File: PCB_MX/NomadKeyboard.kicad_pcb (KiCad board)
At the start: 2 copper layers, 159.9 x 129.6 mm, 97 parts, among them J1 4PIN, J2 OLED, SW1 SW_PUSH_LED, SW10 SW_PUSH_LED, SW11 SW_PUSH_LED, SW12 SW_PUSH_LED, SW13 SW_PUSH_LED, SW14 SW_PUSH_LED, SW15 SW_PUSH_LED, SW16 SW_PUSH_LED, SW17 SW_PUSH_LED, SW18 SW_PUSH_LED, SW19 SW_PUSH_LED, SW2 SW_PUSH_LED, SW20 SW_PUSH_LED, SW21 SW_PUSH_LED, SW22 SW_PUSH_LED, SW23 SW_PUSH_LED, SW24 SW_PUSH_LED, SW25 SW_PUSH_LED, SW26 SW_PUSH_LED, SW27 SW_PUSH_LED, SW28 SW_PUSH_LED, SW29 SW_PUSH_LED, SW3 SW_PUSH_LED, SW30 SW_PUSH_LED, SW31 SW_PUSH_LED, SW32 SW_PUSH_LED, SW33 SW_PUSH_LED, SW34 SW_PUSH_LED, SW4 SW_PUSH_LED, SW5 SW_PUSH_LED, SW6 SW_PUSH_LED, SW7 SW_PUSH_LED, SW8 SW_PUSH_LED, SW9 SW_PUSH_LED, U1 ProMicro

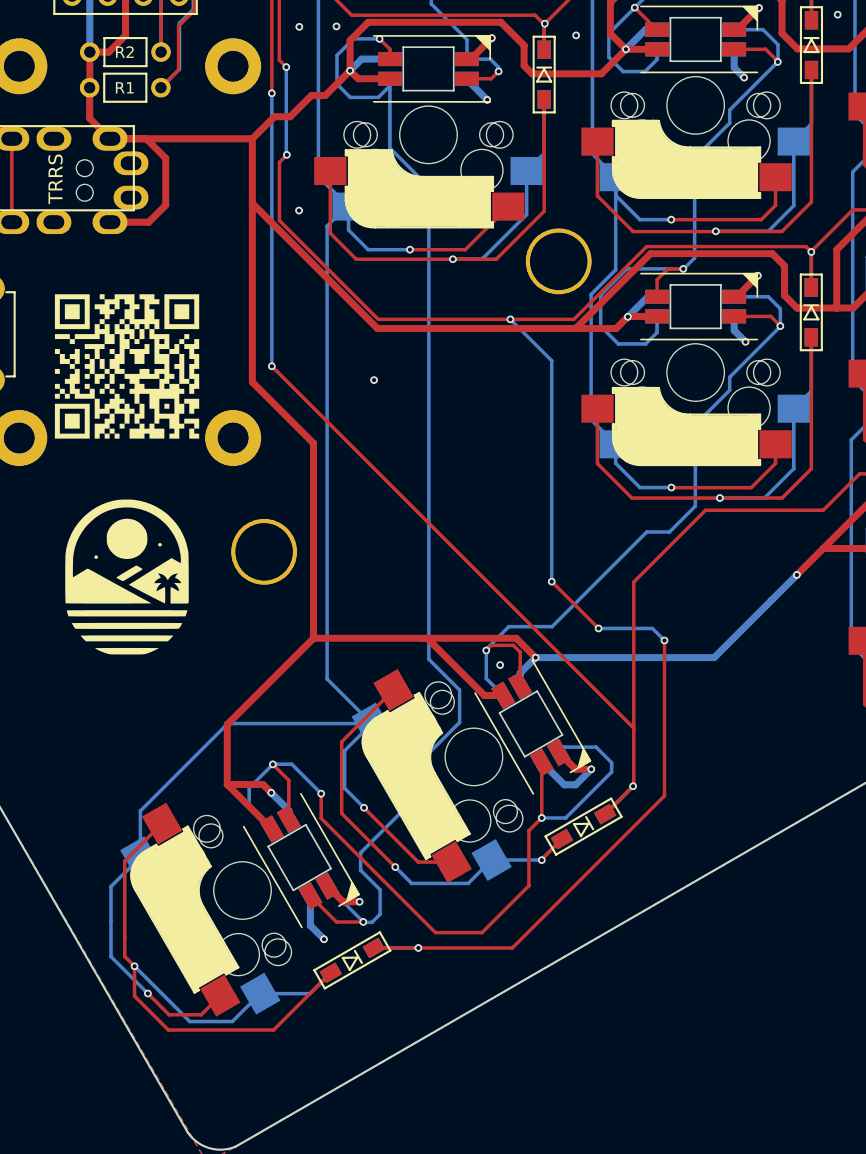
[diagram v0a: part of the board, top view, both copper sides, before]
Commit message: Rotated thumb cluster keys on the MX version for 1.5U shine-through blank key caps
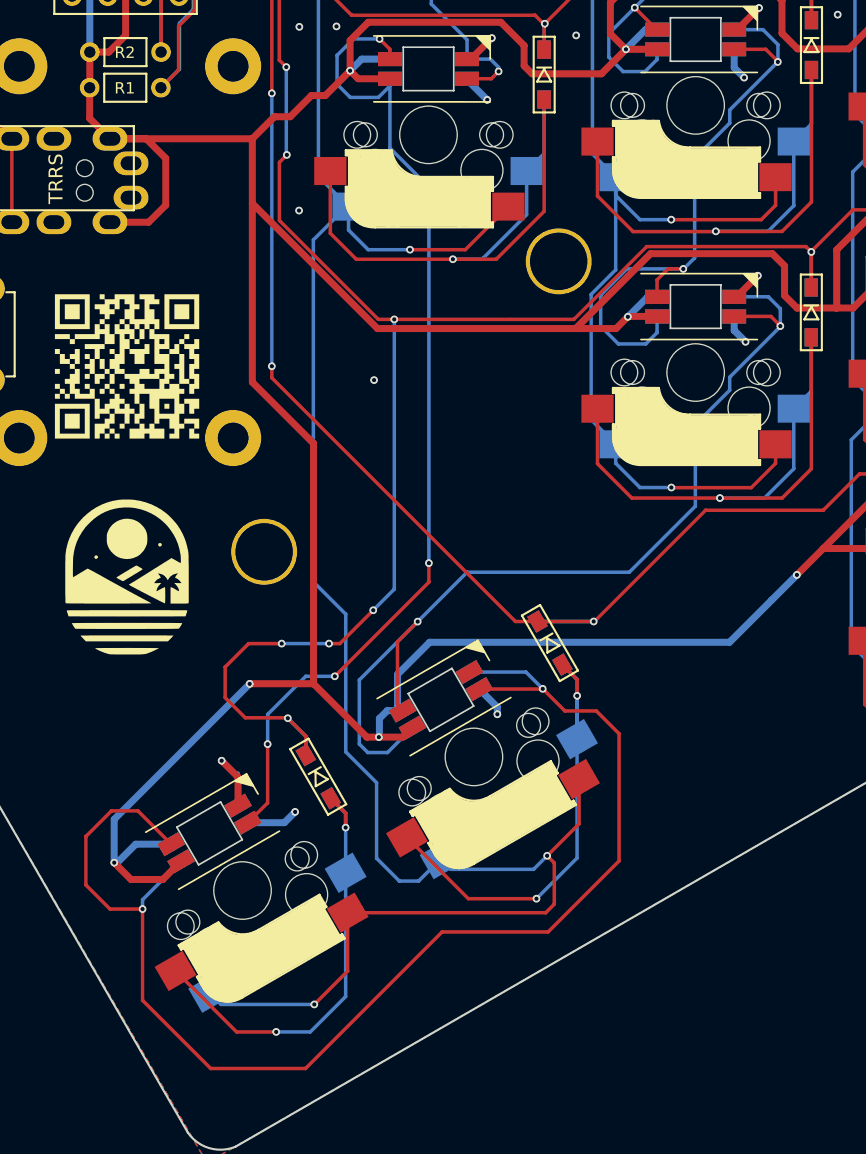
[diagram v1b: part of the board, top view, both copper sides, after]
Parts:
- moved D22 13.3 mm to (93.6, 136.0), turned to -60 degrees
- moved D29 13.3 mm to (110.1, 126.4), turned to -60 degrees
- turned SW22 to -150 degrees
- turned SW29 to -150 degrees
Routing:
- net Net-(SW22B-DOUT): track 56.5 -> 95.3 mm, vias 3 -> 2
- net ROW3: track 284.9 -> 262.9 mm
- net ROW4: track 247.1 -> 229.4 mm
- net Net-(SW23B-DIN): track 51.9 -> 69.3 mm
- net Net-(D22-A): track 47.4 -> 32.1 mm, vias 1 -> 2
- net Net-(SW15B-DOUT): track 86.6 -> 74.9 mm, vias 2 -> 4
- net VCC: track 1349.3 -> 1360.3 mm, vias 49 -> 50
- net COL6: track 206.3 -> 215.8 mm
- net Net-(D29-A): track 31.5 -> 38.2 mm
- net GND: track 180.0 -> 176.0 mm, vias 125 -> 124

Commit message: Update Gerber files for MX version
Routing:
- net Net-(SW15B-DOUT): track 74.9 -> 77.9 mm
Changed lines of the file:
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@@
+	)
+	(segment
+		(start 87.91027 135.71149)
+		(end 87.96027 135.71149)
+		(width 0.25)
+		(layer "B.Cu")
+		(net 63)
 	)
 	(segment
@@
 		(width 0.25)
 		(layer "B.Cu")
+		(net 63)
+	)
+	(segment
+		(start 87.96027 135.71149)
+		(end 90.01912 133.65264)
+		(width 0.25)
+		(layer "B.Cu")

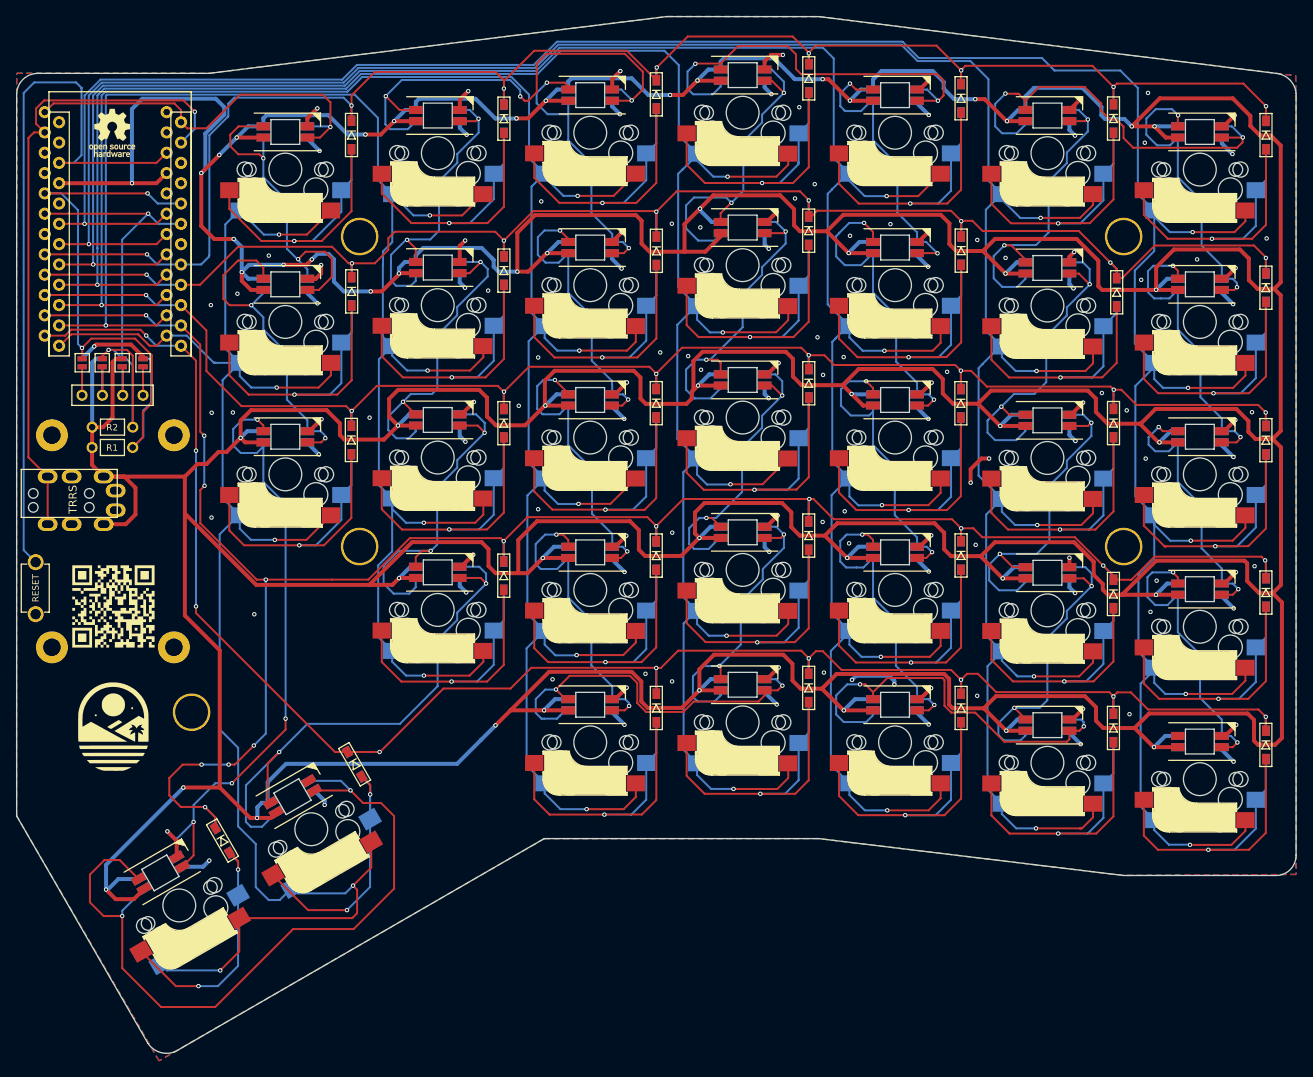
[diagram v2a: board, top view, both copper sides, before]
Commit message: Nomad Rev 2
* Exclusively supports RP2040 CE microcontrollers
* Only one set of headers for hte RP2040 with solder jumpers to select
  the half
* EC12 low-profile rotary encoder support
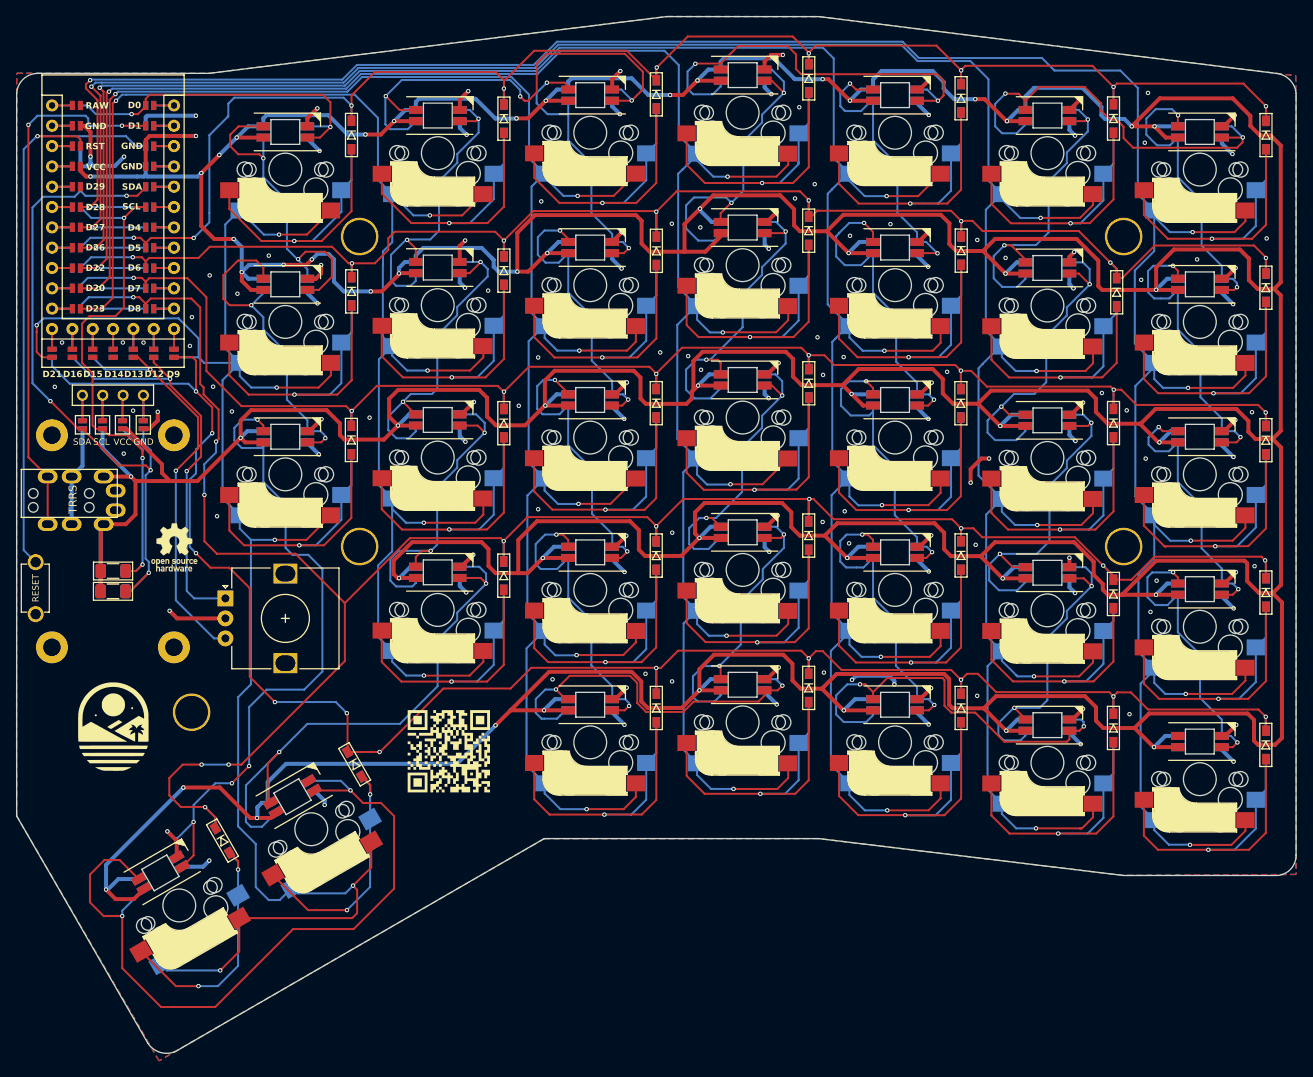
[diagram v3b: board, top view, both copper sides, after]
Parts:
- removed U1: ProMicro, SofleChoc:ProMicro
- added RE1: RotaryEncoder, Rotary_Encoder:RotaryEncoder_Alps_EC12E_Vertical_H20mm, F.Cu at (94.0, 105.7)
- added RP2040_CE1: ~, Nomad:RP2040_CE, F.Cu at (80.0, 57.8)
- R1, R2: footprint SofleChoc:RESISTOR_mini -> Nomad:R_1206_3216Metric_Pad1.30x1.75mm_HandSolder
- moved OH2 52.4 mm to (87.6, 99.3)
- moved OH1 52.4 mm to (87.6, 99.3)
- moved QR2 45.7 mm to (121.9, 124.8)
- moved QR1 45.7 mm to (121.9, 124.8)
- moved R1 18.0 mm to (79.9, 104.8)
- moved R2 18.0 mm to (80.0, 102.3)
- moved JP1 7.76 mm to (83.7, 84.0), turned to -90 degrees
- moved JP2 7.76 mm to (81.1, 84.0), turned to -90 degrees
- moved JP3 7.76 mm to (78.6, 84.0), turned to -90 degrees
- moved JP4 7.76 mm to (76.1, 84.0), turned to -90 degrees
- moved JP5 7.75 mm to (83.7, 84.0), turned to -90 degrees
- moved JP6 7.75 mm to (81.1, 84.0), turned to -90 degrees
- moved JP7 7.75 mm to (78.6, 84.0), turned to -90 degrees
- moved JP8 7.75 mm to (76.1, 84.0), turned to -90 degrees
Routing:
- net VCC: track 1360.3 -> 1262.2 mm, vias 50 -> 51
- net ENCB: track 0.00 -> 51.2 mm, vias 0 -> 2
- net ENCA: track 0.00 -> 51.0 mm, vias 0 -> 2
- net GND: track 176.0 -> 221.5 mm, vias 124 -> 136
- net RESET: track 92.9 -> 75.1 mm, vias 0 -> 1
- net DATA: track 80.5 -> 68.2 mm, vias 1 -> 2
- net ROW4: track 229.4 -> 239.2 mm, vias 9 -> 11
- net SCL: track 62.3 -> 71.3 mm, vias 2 -> 3
- net COL5: track 209.6 -> 200.8 mm, vias 5 -> 6
- net COL4: track 265.8 -> 257.1 mm, vias 6 -> 7
- net COL3: track 286.9 -> 278.5 mm, vias 6 -> 7
- net COL6: track 215.8 -> 223.8 mm, vias 5 -> 6
- net SDA: track 76.9 -> 84.6 mm, vias 2 -> 4
- net COL2: track 309.5 -> 301.9 mm, vias 6 -> 7
- net ROW3: track 262.9 -> 270.2 mm, vias 14 -> 12
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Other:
- board text added: "GND"
- board text added: "SCL"
- board text added: "SDA"
- board text added: "VCC"
